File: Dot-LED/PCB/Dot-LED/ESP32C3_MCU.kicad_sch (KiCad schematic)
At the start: 23 parts, among them IC1 ESP32-C3, Y1 32.768Khz, Y2 RH100-40.000-12-F-1010-TR

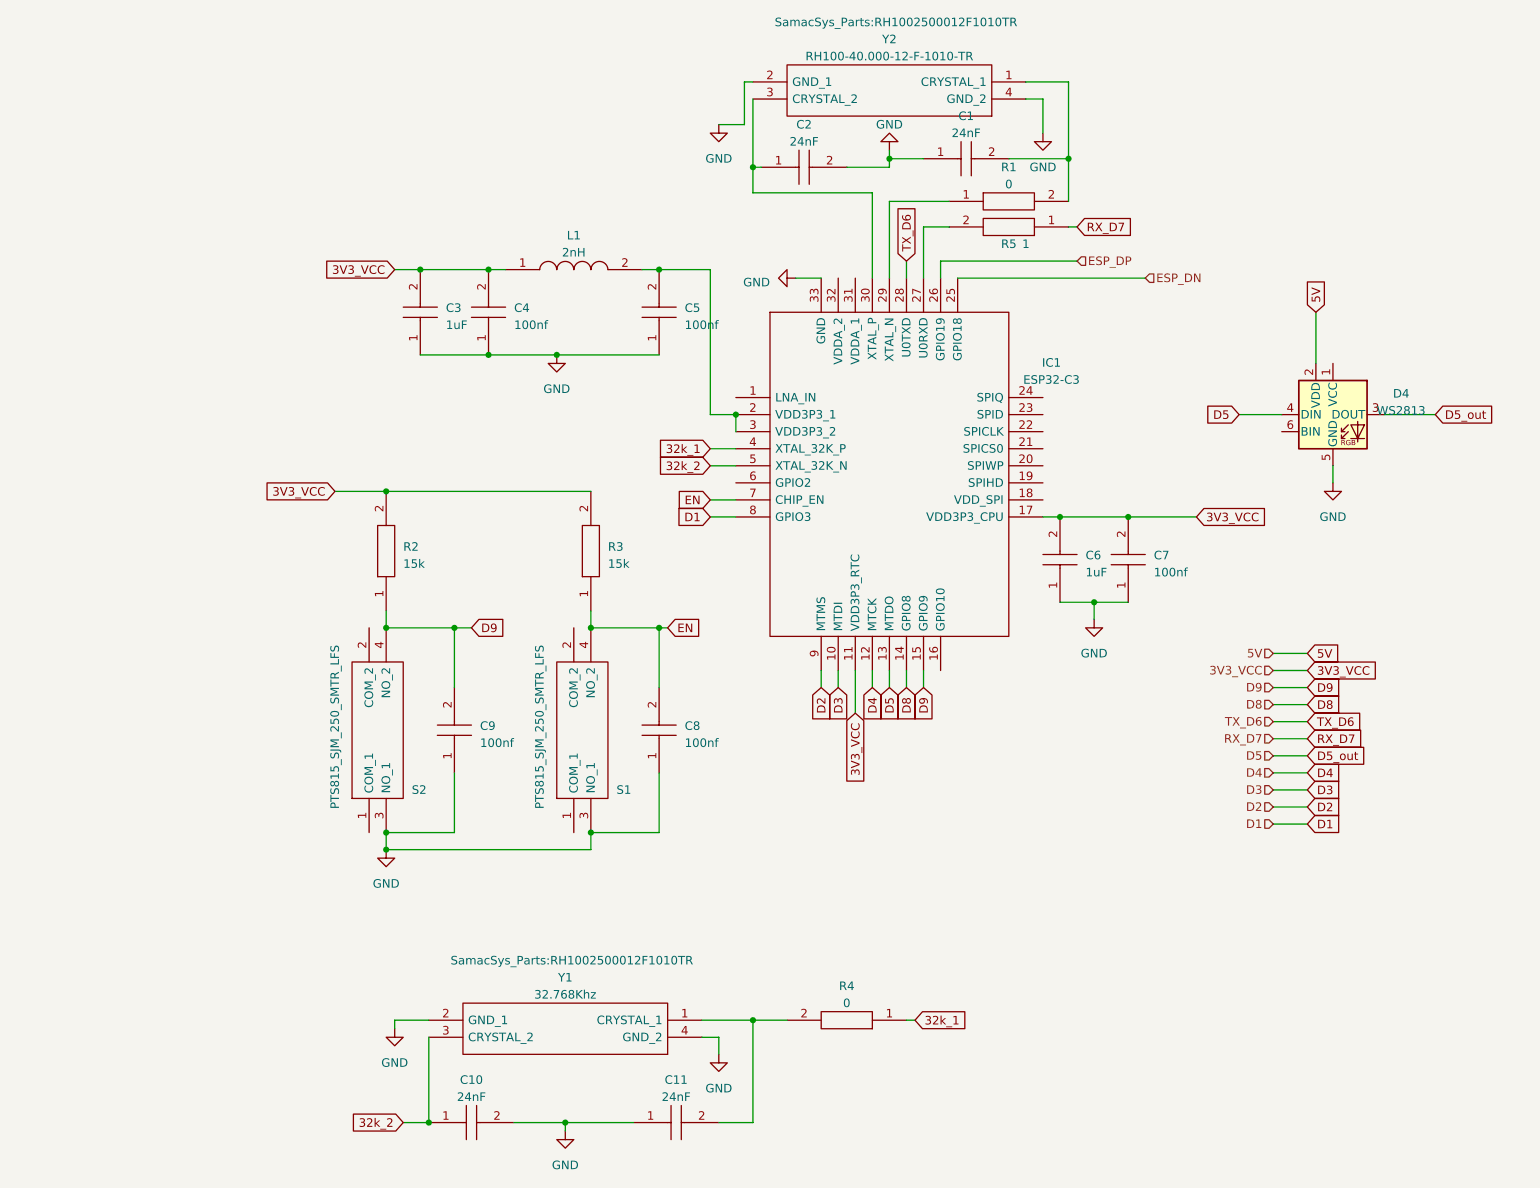
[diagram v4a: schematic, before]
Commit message: Init layout for DotLED
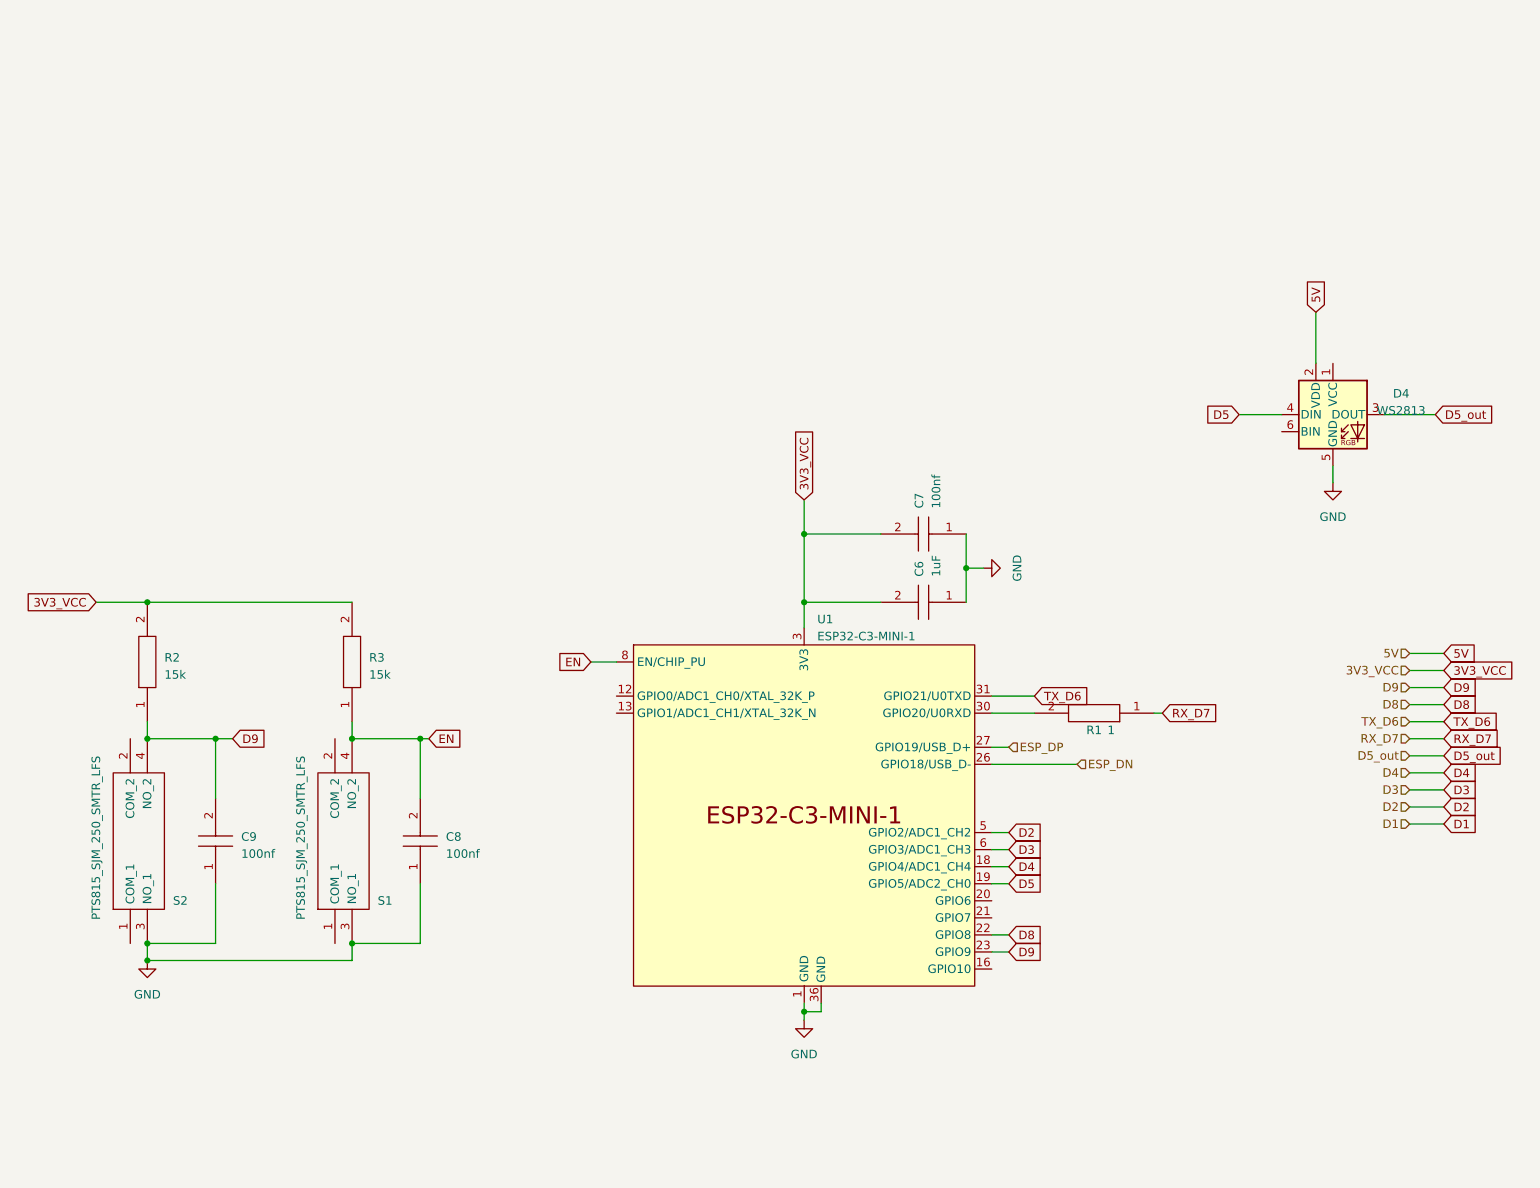
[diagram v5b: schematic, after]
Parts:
- removed C1, C10, C11, C2: 24nF, SamacSys_Parts:CAPC1005X55N, symbol SamacSys_Parts:0402B102K500NT
- removed C3: 1uF, Capacitor_SMD:C_0603_1608Metric_Pad1.08x0.95mm_HandSolder, symbol SamacSys_Parts:0402B102K500NT
- removed C4, C5: 100nf, Capacitor_SMD:C_0603_1608Metric_Pad1.08x0.95mm_HandSolder, symbol SamacSys_Parts:0402B102K500NT
- removed IC1: ESP32-C3, QFN50P500X500X90-33N-D, symbol SamacSys_Parts:ESP32-C3
- removed L1: 2nH, LQG15WH0N7B02D, symbol SamacSys_Parts:LQG15HN2N0S02D
- removed R4: 0, RESC1608X55N, symbol SamacSys_Parts:RMCF0603ZT0R00
- removed R5: 1, RESC1608X55N, symbol SamacSys_Parts:RMCF0603ZT0R00
- removed Y1: 32.768Khz, SamacSys_Parts:RH1002500012F1010TR, symbol SamacSys_Parts:RH100-25.000-12-F-1010-TR
- removed Y2: RH100-40.000-12-F-1010-TR, SamacSys_Parts:RH1002500012F1010TR, symbol SamacSys_Parts:RH100-25.000-12-F-1010-TR
- added U1: ESP32-C3-MINI-1, Espressif:ESP32-C3-MINI-1U, symbol Espressif:ESP32-C3-MINI-1
- R1: value 0 -> 1; Digi-Key_PN 708-RMCF0603ZT0R00 -> (none); Manufacturer_Name Stackpole Electronics, Inc. -> (none); Manufacturer_Part_Number RMCF0603ZT0R00 -> (none); Mouser Part Number 708-RMCF0603ZT0R00 -> (none); Mouser Price/Stock https://www.mouser.co.uk/ProductDetail/SEI-Stackpole/RMCF06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 -> (none)
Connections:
- net 3V3_VCC: now also U1.3 (3V3)
- net D2: now also U1.5 (GPIO2/ADC1_CH2)
- net D3: now also U1.6 (GPIO3/ADC1_CH3)
- net D4: now also U1.18 (GPIO4/ADC1_CH4)
- net D5: now also U1.19 (GPIO5/ADC2_CH0); no longer D4.3 (DOUT)
- net D8: now also U1.22 (GPIO8)
- net D9: now also U1.23 (GPIO9)
- net EN: now also U1.8 (EN/CHIP_PU)
- net ESP_DN: now also U1.26 (GPIO18/USB_D-)
- net ESP_DP: now also U1.27 (GPIO19/USB_D+)
- net GND: now also U1.36 (GND), U1.37 (GND), U1.38 (GND), U1.39 (GND), U1.40 (GND), U1.41 (GND), U1.42 (GND), U1.43 (GND), U1.44 (GND), U1.45 (GND), U1.46 (GND), U1.47 (GND), U1.48 (GND), U1.49 (GND), U1.50 (GND), U1.51 (GND), U1.52 (GND), U1.53 (GND)
- net RX_D7: now also R1.1
- net TX_D6: now also U1.31 (GPIO21/U0TXD)
- net at R1.2: now also U1.30 (GPIO20/U0RXD)
- new net: U1.1 (GND), U1.11 (GND), U1.14 (GND), U1.2 (GND)
- new net D5_out: D4.3 (DOUT)
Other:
- moved on the sheet: C6, C7, C8, C9, R2, R3, S1, S2

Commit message: Update Vreg to in-stock component
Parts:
- C6: LCSC Part Number (none) -> C15849
- C7, C8, C9: LCSC Part Number (none) -> C14663
- D4: LCSC Part Number (none) -> C114592
- R2, R3: LCSC Part Number (none) -> C22809
- S1, S2: LCSC Part Number (none) -> C411883
- U1: LCSC Part Number (none) -> C2911374
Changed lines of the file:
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@@
       (effects (font (size 1.27 1.27)) (justify left top) hide)
+    )
+    (property "LCSC Part Number" "C114592" (at 210.82 71.12 0)
+      (effects (font (size 1.27 1.27)) hide)
     )
     (pin "1")
@@
       (effects (font (size 1.27 1.27)) (justify left) hide)
     )
+    (property "LCSC Part Number" "C22809" (at 34.29 116.84 0)
+      (effects (font (size 1.27 1.27)) hide)
+    )
     (pin "1")
     (pin "2")
@@
       (effects (font (size 1.27 1.27)) hide)
     )
+    (property "LCSC Part Number" "C411883" (at 62.23 149.86 0)
+      (effects (font (size 1.27 1.27)) hide)
+    )
     (pin "1")
     (pin "2")
@@
     (property "Arrow Price/Stock" "" (at 147.32 67.31 0)
       (effects (font (size 1.27 1.27)) (justify left) hide)
+    )
+    (property "LCSC Part Number" "C14663" (at 156.21 88.9 0)
+      (effects (font (size 1.27 1.27)) hide)
     )
     (pin "1")
@@
       (effects (font (size 1.27 1.27)) (justify left) hide)
     )
+    (property "LCSC Part Number" "" (at 184.15 115.57 0)
+      (effects (font (size 1.27 1.27)) hide)
+    )
     (pin "1")
     (pin "2")
@@
       (effects (font (size 1.27 1.27)) hide)
     )
+    (property "LCSC Part Number" "C411883" (at 31.75 149.86 0)
+      (effects (font (size 1.27 1.27)) hide)
+    )
     (pin "1")
     (pin "2")
@@
       (effects (font (size 1.27 1.27)) (justify left) hide)
     )
+    (property "LCSC Part Number" "C14663" (at 44.45 140.97 0)
+      (effects (font (size 1.27 1.27)) hide)
+    )
     (pin "1")
     (pin "2")
@@
     )
     (property "Digi-Key_PN" "1276-1102-1-ND" (at 156.21 99.06 0)
+      (effects (font (size 1.27 1.27)) hide)
+    )
+    (property "LCSC Part Number" "C15849" (at 156.21 99.06 0)
       (effects (font (size 1.27 1.27)) hide)
     )
@@
       (effects (font (size 1.27 1.27)) (justify left) hide)
     )
+    (property "LCSC Part Number" "C22809" (at 64.77 116.84 0)
+      (effects (font (size 1.27 1.27)) hide)
+    )
     (pin "1")
     (pin "2")
@@
     )
     (property "Datasheet" "https://www.espressif.com/sites/default/files/documentation/esp32-c3-mini-1_datasheet_en.pdf" (at 132.08 168.91 0)
+      (effects (font (size 1.27 1.27)) hide)
+    )
+    (property "LCSC Part Number" "C2911374" (at 132.08 130.81 0)
       (effects (font (size 1.27 1.27)) hide)
     )
@@
       (effects (font (size 1.27 1.27)) (justify left) hide)
     )
-    (pin "1")
+    (property "LCSC Part Number" "C14663" (at 74.93 140.97 0)
+      (effects (font (size 1.27 1.27)) hide)
+    )
+    (pin "1")

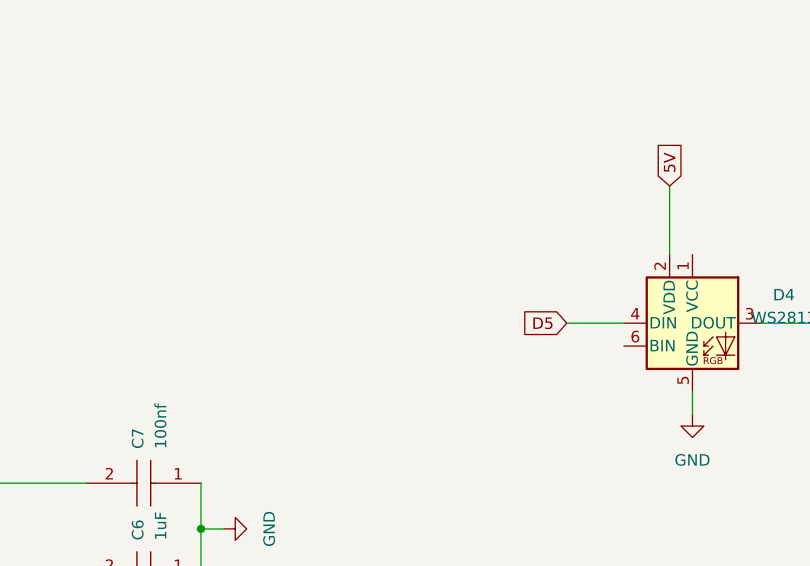
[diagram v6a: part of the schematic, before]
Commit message: finalize design based on in-stock parts
Gerber out 1.0
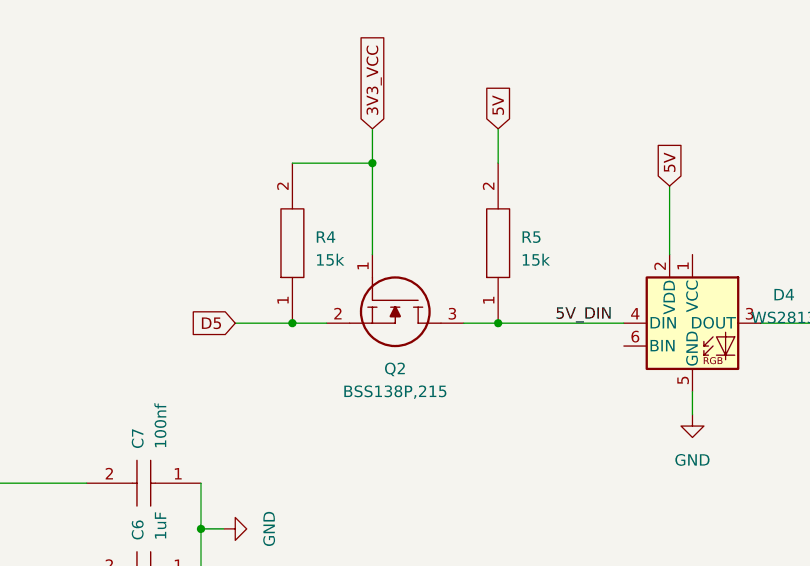
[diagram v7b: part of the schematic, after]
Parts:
- added Q2: BSS138P,215, SamacSys_Parts:SOT95P230X110-3N, symbol SamacSys_Parts:BSS138P,215
- added R4, R5: 15k, RESC1608X55N, symbol SamacSys_Parts:RMCF0603ZT0R00
- C6: MPN (none) -> C15849
- C7, C8, C9: MPN (none) -> C14663
- D4: MPN (none) -> C114592
- R1: LCSC Part Number (none) -> C247057; MPN (none) -> C247057
- R2, R3: MPN (none) -> C22809
- S1, S2: MPN (none) -> C411883
- U1: MPN (none) -> C2911374
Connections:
- net 3V3_VCC: now also Q2.1, R4.2
- net 5V: now also R5.2
- net D5: now also Q2.2, R4.1; no longer D4.4 (DIN)
- new net 5V_DIN: D4.4 (DIN), Q2.3, R5.1

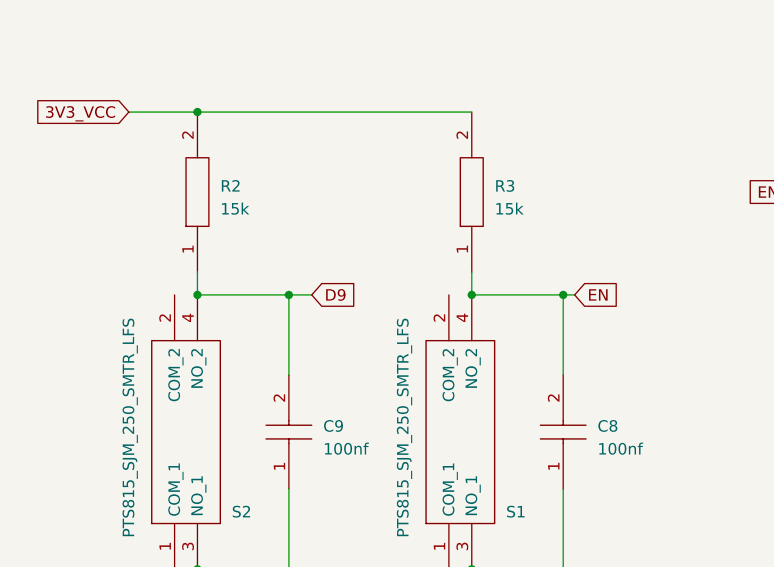
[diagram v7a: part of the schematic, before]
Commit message: added code for inital wled stuff
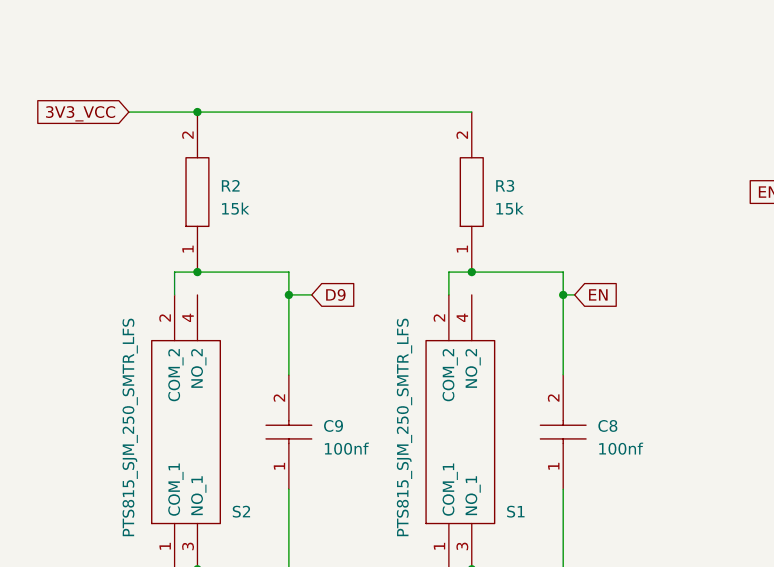
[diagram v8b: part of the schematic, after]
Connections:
- net D9: now also S2.2 (COM_2); no longer S2.4 (NO_2)
- net EN: now also S1.2 (COM_2); no longer S1.4 (NO_2)
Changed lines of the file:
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@@
   (junction (at 175.26 53.34) (diameter 0) (color 0 0 0 0)
   )
+  (junction (at 34.29 116.84) (diameter 0) (color 0 0 0 0)
+  )
+  (junction (at 166.37 71.12) (diameter 0) (color 0 0 0 0)
+  )
+  (junction (at 132.08 88.9) (diameter 0) (color 0 0 0 0)
+  )
+  (junction (at 34.29 99.06) (diameter 0) (color 0 0 0 0)
+  )
   (junction (at 74.93 119.38) (diameter 0) (color 0 0 0 0)
   )
-  (junction (at 166.37 71.12) (diameter 0) (color 0 0 0 0)
-  )
-  (junction (at 132.08 88.9) (diameter 0) (color 0 0 0 0)
-  )
-  (junction (at 34.29 99.06) (diameter 0) (color 0 0 0 0)
-  )
   (junction (at 132.08 99.06) (diameter 0) (color 0 0 0 0)
   )
-  (junction (at 64.77 119.38) (diameter 0) (color 0 0 0 0)
+  (junction (at 64.77 116.84) (diameter 0) (color 0 0 0 0)
+  )
+  (junction (at 34.29 149.86) (diameter 0) (color 0 0 0 0)
   )
   (junction (at 44.45 119.38) (diameter 0) (color 0 0 0 0)
   )
-  (junction (at 34.29 119.38) (diameter 0) (color 0 0 0 0)
-  )
-  (junction (at 34.29 149.86) (diameter 0) (color 0 0 0 0)
-  )
   (wire (pts (xy 132.08 160.02) (xy 134.62 160.02))
     (stroke (width 0) (type default))
@@
     (stroke (width 0) (type default))
   )
-  (wire (pts (xy 34.29 116.84) (xy 34.29 119.38))
+  (wire (pts (xy 34.29 116.84) (xy 44.45 116.84))
     (stroke (width 0) (type default))
   )
@@
     (stroke (width 0) (type default))
   )
-  (wire (pts (xy 44.45 119.38) (xy 34.29 119.38))
+  (wire (pts (xy 64.77 116.84) (xy 74.93 116.84))
     (stroke (width 0) (type default))
   )
@@
     (stroke (width 0) (type default))
   )
+  (wire (pts (xy 44.45 119.38) (xy 44.45 116.84))
+    (stroke (width 0) (type default))
+  )
   (wire (pts (xy 222.25 119.38) (xy 227.33 119.38))
     (stroke (width 0) (type default))
@@
     (stroke (width 0) (type default))
   )
+  (wire (pts (xy 31.75 119.38) (xy 31.75 116.84))
+    (stroke (width 0) (type default))
+  )
   (wire (pts (xy 160.02 123.19) (xy 172.72 123.19))
     (stroke (width 0) (type default))
   )
+  (wire (pts (xy 62.23 119.38) (xy 62.23 116.84))
+    (stroke (width 0) (type default))
+  )
   (wire (pts (xy 160.02 71.12) (xy 166.37 71.12))
     (stroke (width 0) (type default))
   )
-  (wire (pts (xy 74.93 119.38) (xy 64.77 119.38))
-    (stroke (width 0) (type default))
-  )
   (wire (pts (xy 222.25 124.46) (xy 227.33 124.46))
     (stroke (width 0) (type default))
@@
     (stroke (width 0) (type default))
   )
+  (wire (pts (xy 74.93 116.84) (xy 74.93 119.38))
+    (stroke (width 0) (type default))
+  )
   (wire (pts (xy 175.26 49.53) (xy 175.26 53.34))
     (stroke (width 0) (type default))
@@
     (stroke (width 0) (type default))
   )
-  (wire (pts (xy 64.77 116.84) (xy 64.77 119.38))
-    (stroke (width 0) (type default))
-  )
+  (wire (pts (xy 31.75 116.84) (xy 34.29 116.84))
+    (stroke (width 0) (type default))
+  )
+  (wire (pts (xy 62.23 116.84) (xy 64.77 116.84))
+    (stroke (width 0) (type default))
+  )
